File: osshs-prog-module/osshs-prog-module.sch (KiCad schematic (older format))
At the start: 2 parts, among them U1 STM32F103RETx

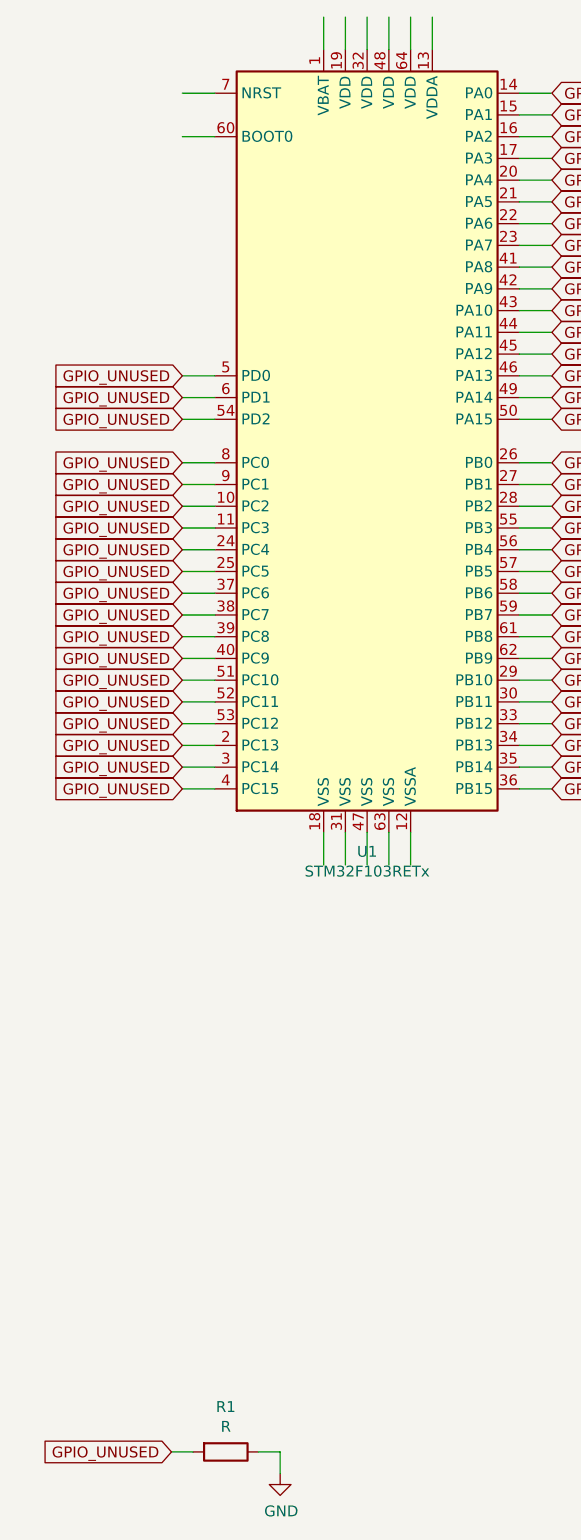
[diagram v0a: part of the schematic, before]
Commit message: [osshs-prog-module] Add reset circuit
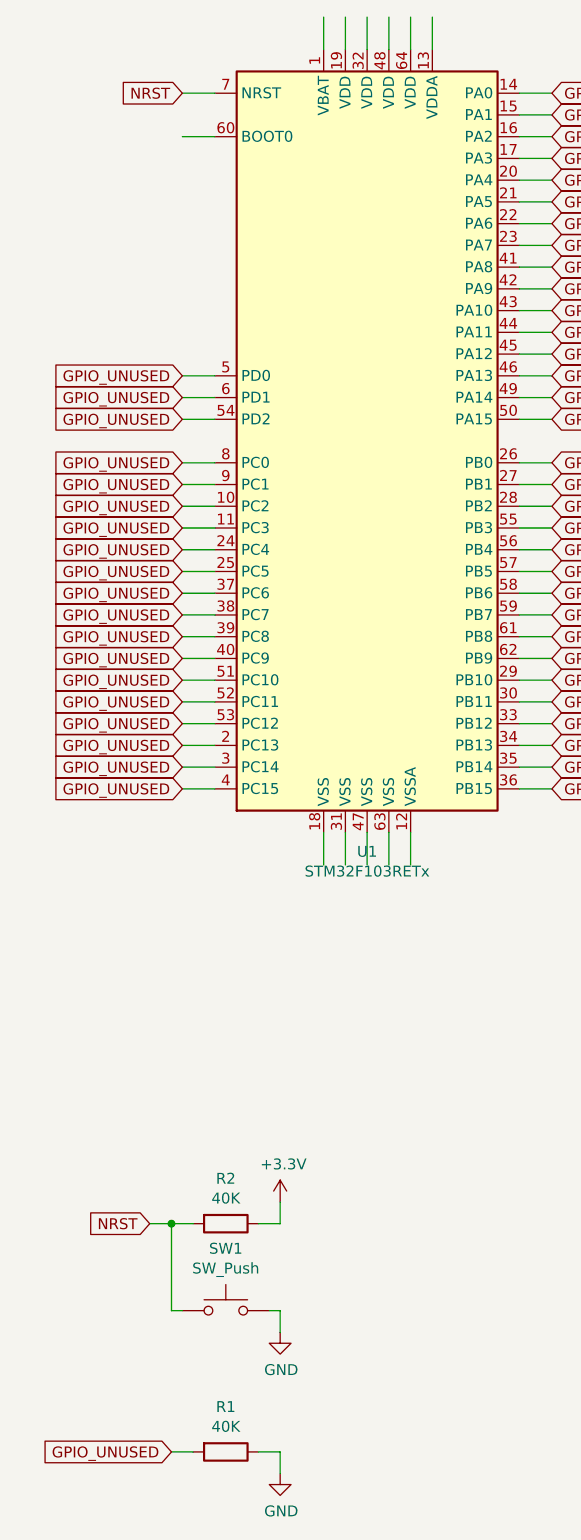
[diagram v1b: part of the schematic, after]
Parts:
- added R2: 40K, Resistor_SMD:R_0805_2012Metric, symbol Device:R
- added SW1: SW_Push, Button_Switch_SMD:SW_SPST_B3U-1000P, symbol Switch:SW_Push
- R1: value R -> 40K; footprint (none) -> Resistor_SMD:R_0805_2012Metric
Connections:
- net labels added: +3.3V, NRST
- wire segments 67 -> 75
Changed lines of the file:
@@
 EESchema Schematic File Version 4
+LIBS:osshs-prog-module-cache
 EELAYER 30 0
 EELAYER END
@@
 GPIO_UNUSED
 $Comp
+L Device:R R1
+U 1 1 5DEAE2F3
+P 1350 7450
+F 0 "R1" V 1143 7450 50  0000 C CNN
+F 1 "40K" V 1234 7450 50  0000 C CNN
+F 2 "Resistor_SMD:R_0805_2012Metric" V 1280 7450 50  0001 C CNN
+F 3 "~" H 1350 7450 50  0001 C CNN
+	1    1350 7450
+	0    1    1    0
+$EndComp
+Wire Wire Line
+	1100 7450 1200 7450
+Wire Wire Line
+	1500 7450 1600 7450
+Text GLabel 1150 1200 0    50   Input ~ 0
+NRST
+Text GLabel 1000 6400 0    50   Input ~ 0
+NRST
+$Comp
+L power:+3.3V #PWR0102
+U 1 1 5DE720C2
+P 1600 6300
+F 0 "#PWR0102" H 1600 6150 50  0001 C CNN
+F 1 "+3.3V" H 1615 6473 50  0000 C CNN
+F 2 "" H 1600 6300 50  0001 C CNN
+F 3 "" H 1600 6300 50  0001 C CNN
+	1    1600 6300
+	1    0    0    -1
+$EndComp
+$Comp
+L Device:R R2
+U 1 1 5DE7D093
+P 1350 6400
+F 0 "R2" V 1143 6400 50  0000 C CNN
+F 1 "40K" V 1234 6400 50  0000 C CNN
+F 2 "Resistor_SMD:R_0805_2012Metric" V 1280 6400 50  0001 C CNN
+F 3 "~" H 1350 6400 50  0001 C CNN
+	1    1350 6400
+	0    1    1    0
+$EndComp
+Wire Wire Line
+	1500 6400 1600 6400
+Wire Wire Line
+	1600 6400 1600 6300
+Wire Wire Line
+	1000 6400 1100 6400
+Connection ~ 1100 6400
+Wire Wire Line
+	1100 6400 1200 6400
+$Comp
+L Switch:SW_Push SW1
+U 1 1 5DE869D3
+P 1350 6800
+F 0 "SW1" H 1350 7085 50  0000 C CNN
+F 1 "SW_Push" H 1350 6994 50  0000 C CNN
+F 2 "Button_Switch_SMD:SW_SPST_B3U-1000P" H 1350 7000 50  0001 C CNN
+F 3 "~" H 1350 7000 50  0001 C CNN
+	1    1350 6800
+	1    0    0    -1
+$EndComp
+Wire Wire Line
+	1100 6800 1150 6800
+Wire Wire Line
+	1100 6400 1100 6800
+Wire Wire Line
+	1550 6800 1600 6800
+Wire Wire Line
+	1600 6800 1600 6900
+Wire Wire Line
+	1600 7450 1600 7550
+$Comp
 L power:GND #PWR0101
 U 1 1 5DEA1645
@@
 $EndComp
 $Comp
-L Device:R R1
-U 1 1 5DEAE2F3
-P 1350 7450
-F 0 "R1" V 1143 7450 50  0000 C CNN
-F 1 "R" V 1234 7450 50  0000 C CNN
-F 2 "" V 1280 7450 50  0001 C CNN
-F 3 "~" H 1350 7450 50  0001 C CNN
-	1    1350 7450
-	0    1    1    0
-$EndComp
-Wire Wire Line
-	1100 7450 1200 7450
-Wire Wire Line
-	1500 7450 1600 7450
-Wire Wire Line
-	1600 7450 1600 7550
+L power:GND #PWR0103
+U 1 1 5DE92E27
+P 1600 6900
+F 0 "#PWR0103" H 1600 6650 50  0001 C CNN
+F 1 "GND" H 1605 6727 50  0000 C CNN
+F 2 "" H 1600 6900 50  0001 C CNN
+F 3 "" H 1600 6900 50  0001 C CNN
+	1    1600 6900
+	1    0    0    -1
+$EndComp
 $EndSCHEMATC

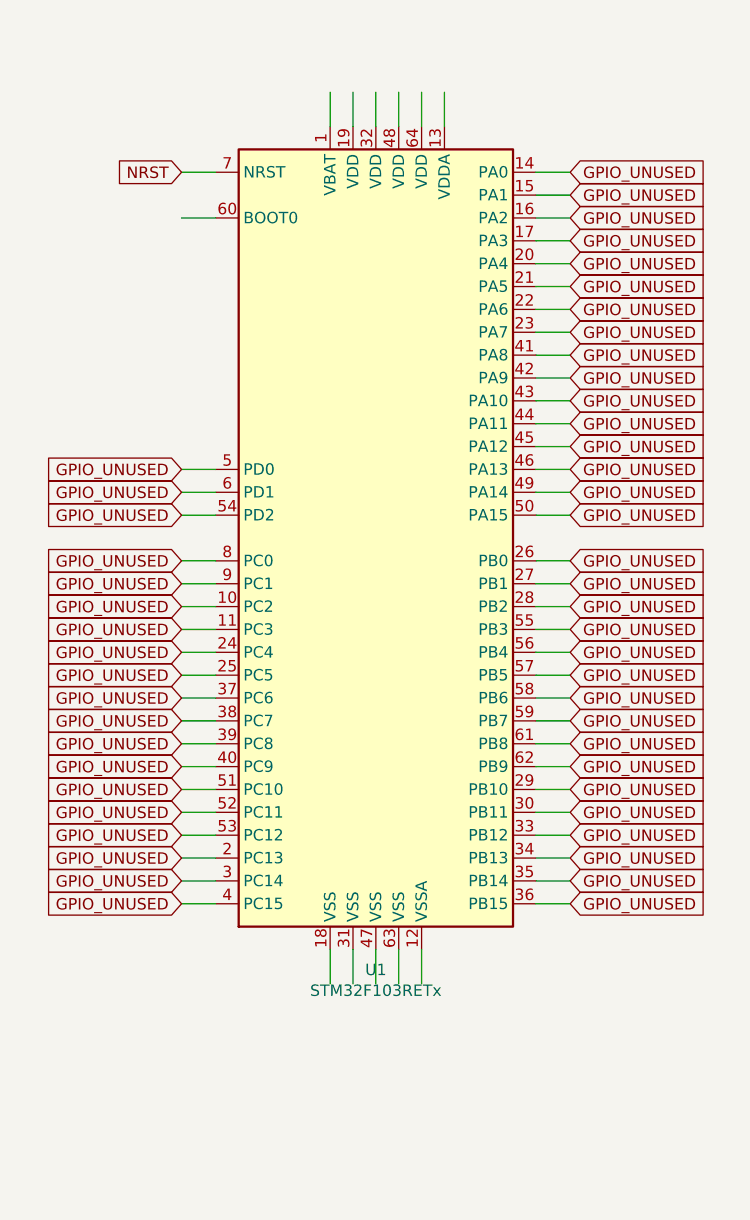
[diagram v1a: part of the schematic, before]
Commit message: [osshs-prog-module] Connect STM32 power pins
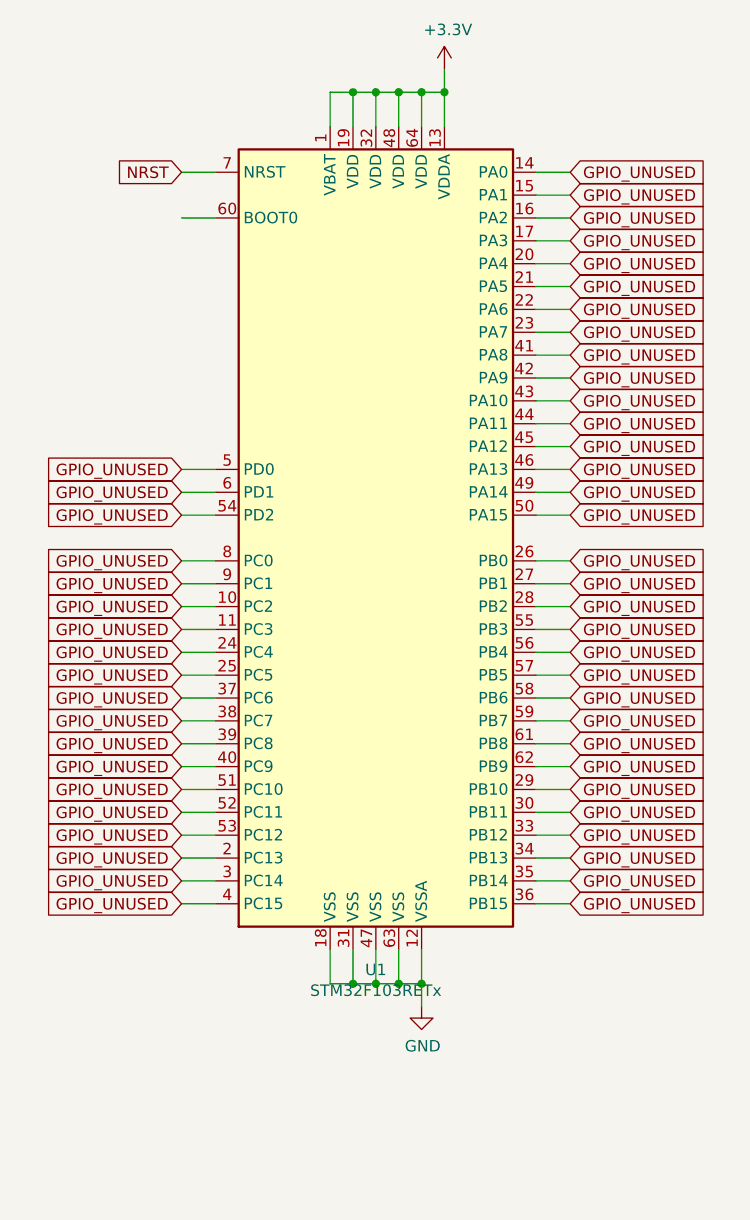
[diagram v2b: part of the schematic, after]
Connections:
- wire segments 75 -> 86
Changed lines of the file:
@@
+	1    0    0    -1
+$EndComp
+Wire Wire Line
+	1800 850  1900 850
+Wire Wire Line
+	1900 850  2000 850
+Connection ~ 1900 850
+Wire Wire Line
+	2000 850  2100 850
+Connection ~ 2000 850
+Wire Wire Line
+	2100 850  2200 850
+Connection ~ 2100 850
+Wire Wire Line
+	2200 850  2300 850
+Connection ~ 2200 850
+Wire Wire Line
+	2300 850  2300 750
+Connection ~ 2300 850
+$Comp
+L power:+3.3V #PWR?
+U 1 1 5DEAFF7F
+P 2300 750
+F 0 "#PWR?" H 2300 600 50  0001 C CNN
+F 1 "+3.3V" H 2315 923 50  0000 C CNN
+F 2 "" H 2300 750 50  0001 C CNN
+F 3 "" H 2300 750 50  0001 C CNN
+	1    2300 750
+	1    0    0    -1
+$EndComp
+Wire Wire Line
+	1800 4750 1900 4750
+Wire Wire Line
+	2000 4750 1900 4750
+Connection ~ 1900 4750
+Wire Wire Line
+	2000 4750 2100 4750
+Connection ~ 2000 4750
+Connection ~ 2100 4750
+Wire Wire Line
+	2100 4750 2200 4750
+Wire Wire Line
+	2200 4750 2200 4850
+Connection ~ 2200 4750
+$Comp
+L power:GND #PWR?
+U 1 1 5DEBBFB0
+P 2200 4850
+F 0 "#PWR?" H 2200 4600 50  0001 C CNN
+F 1 "GND" H 2205 4677 50  0000 C CNN
+F 2 "" H 2200 4850 50  0001 C CNN
+F 3 "" H 2200 4850 50  0001 C CNN
+	1    2200 4850
 	1    0    0    -1
 $EndComp

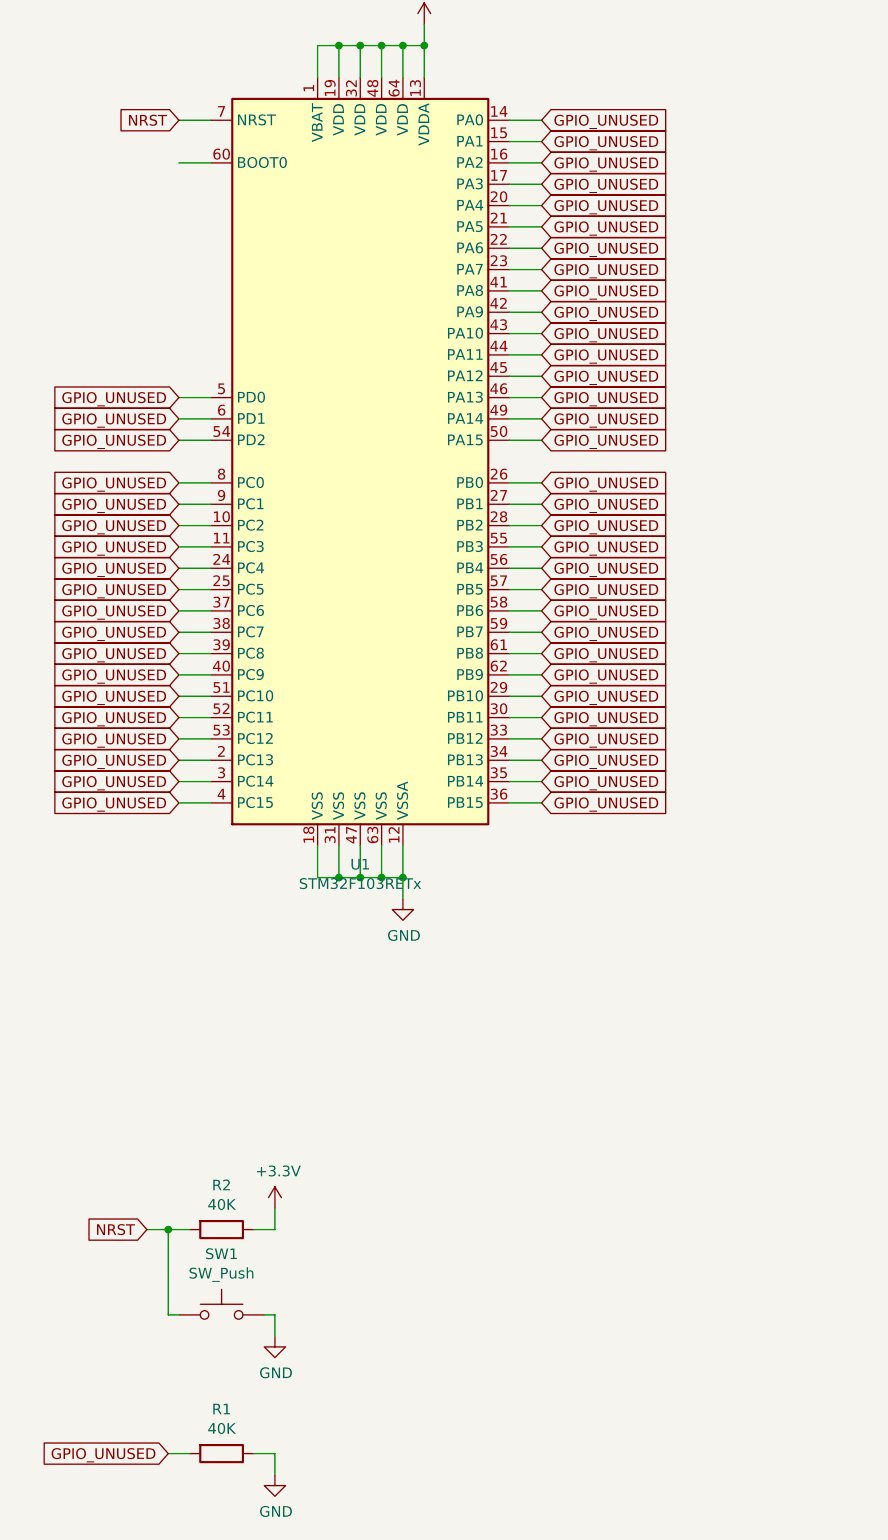
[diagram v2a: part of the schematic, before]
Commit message: [osshs-prog-module] Add boot mode selection circuit
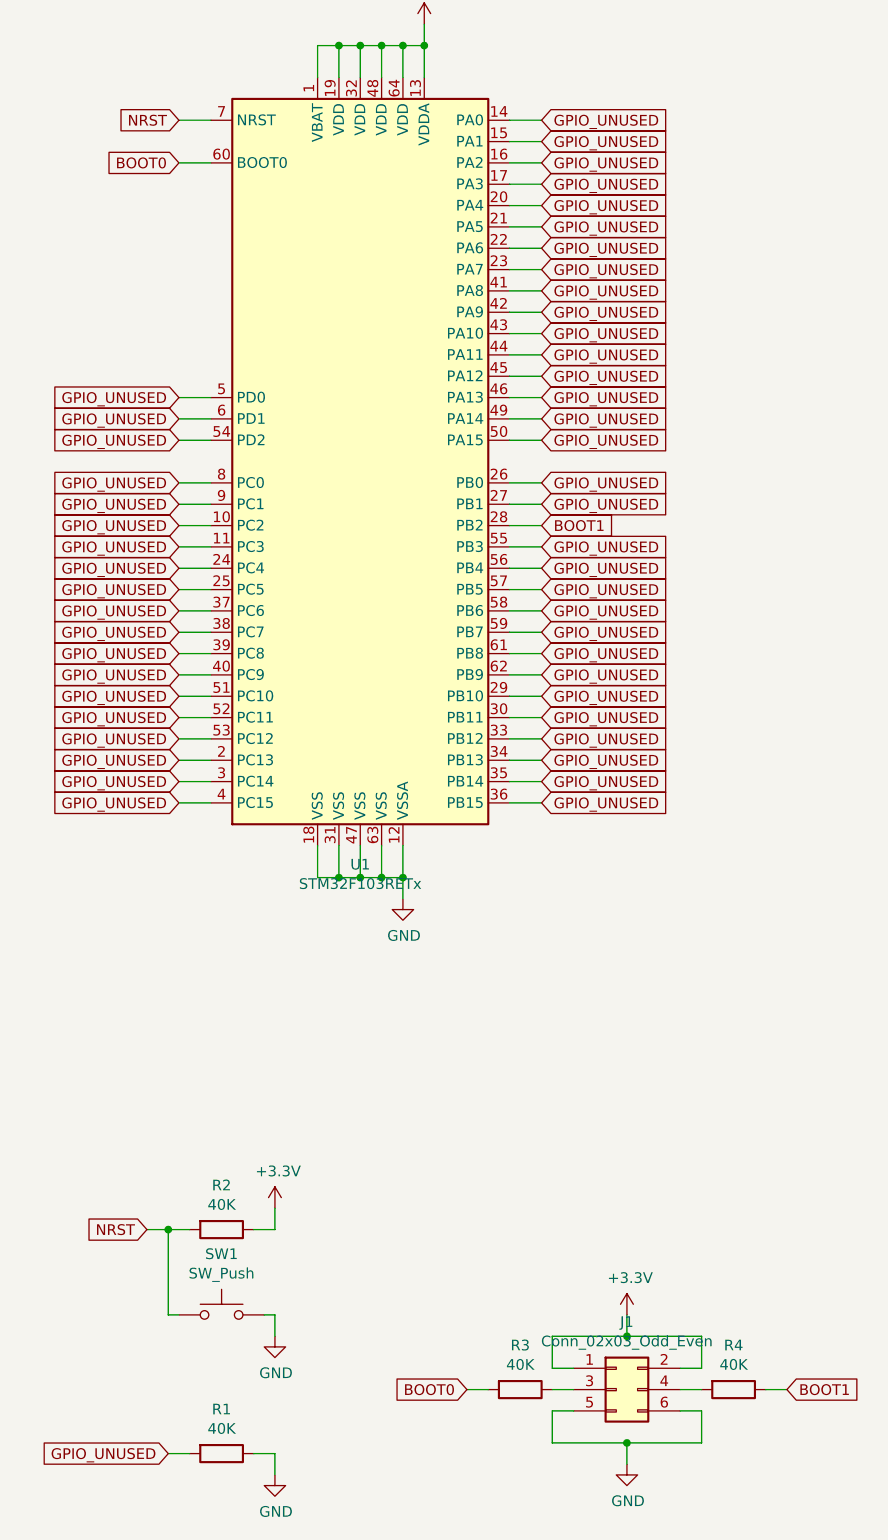
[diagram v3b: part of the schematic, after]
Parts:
- added J1: Conn_02x03_Odd_Even, Connector_PinHeader_2.54mm:PinHeader_2x03_P2.54mm_Vertical, symbol Connector_Generic:Conn_02x03_Odd_Even
- added R3, R4: 40K, Resistor_SMD:R_0805_2012Metric, symbol Device:R
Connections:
- net +3V3: now also J1.1 (Pin_1), J1.2 (Pin_2)
- net GND: now also J1.5 (Pin_5), J1.6 (Pin_6)
- net GPIO_UNUSED: no longer U1.28 (PB2)
- net BOOT0: now reaches U1.60 (BOOT0)
- net BOOT0: now also R3.2
- new net: J1.3 (Pin_3), R3.1
- new net: J1.4 (Pin_4), R4.2
- new net BOOT1: R4.1, U1.28 (PB2)
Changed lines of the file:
@@
 GPIO_UNUSED
 Text GLabel 2850 3100 2    50   Input ~ 0
-GPIO_UNUSED
+BOOT1
 Text GLabel 2850 3200 2    50   Input ~ 0
 GPIO_UNUSED
@@
 Connection ~ 2300 850
 $Comp
-L power:+3.3V #PWR?
+L power:+3.3V #PWR0104
 U 1 1 5DEAFF7F
 P 2300 750
-F 0 "#PWR?" H 2300 600 50  0001 C CNN
+F 0 "#PWR0104" H 2300 600 50  0001 C CNN
 F 1 "+3.3V" H 2315 923 50  0000 C CNN
 F 2 "" H 2300 750 50  0001 C CNN
@@
 Connection ~ 2200 4750
 $Comp
-L power:GND #PWR?
+L power:GND #PWR0105
 U 1 1 5DEBBFB0
 P 2200 4850
-F 0 "#PWR?" H 2200 4600 50  0001 C CNN
+F 0 "#PWR0105" H 2200 4600 50  0001 C CNN
 F 1 "GND" H 2205 4677 50  0000 C CNN
 F 2 "" H 2200 4850 50  0001 C CNN
@@
 	1    0    0    -1
 $EndComp
+Text GLabel 1150 1400 0    50   Input ~ 0
+BOOT0
+$Comp
+L Connector_Generic:Conn_02x03_Odd_Even J1
+U 1 1 5DECC2C7
+P 3200 7150
+F 0 "J1" H 3250 7467 50  0000 C CNN
+F 1 "Conn_02x03_Odd_Even" H 3250 7376 50  0000 C CNN
+F 2 "Connector_PinHeader_2.54mm:PinHeader_2x03_P2.54mm_Vertical" H 3200 7150 50  0001 C CNN
+F 3 "~" H 3200 7150 50  0001 C CNN
+	1    3200 7150
+	1    0    0    -1
+$EndComp
+Wire Wire Line
+	3500 7050 3600 7050
+Wire Wire Line
+	3600 7050 3600 6900
+Wire Wire Line
+	2900 6900 2900 7050
+Wire Wire Line
+	2900 7050 3000 7050
+Wire Wire Line
+	2900 6900 3250 6900
+Wire Wire Line
+	3000 7250 2900 7250
+Wire Wire Line
+	2900 7250 2900 7400
+Wire Wire Line
+	2900 7400 3250 7400
+Wire Wire Line
+	3600 7400 3600 7250
+Wire Wire Line
+	3600 7250 3500 7250
+Wire Wire Line
+	3250 7400 3250 7500
+Connection ~ 3250 7400
+Wire Wire Line
+	3250 7400 3600 7400
+Wire Wire Line
+	3250 6900 3250 6800
+Connection ~ 3250 6900
+Wire Wire Line
+	3250 6900 3600 6900
+$Comp
+L power:+3.3V #PWR0106
+U 1 1 5DED9DD9
+P 3250 6800
+F 0 "#PWR0106" H 3250 6650 50  0001 C CNN
+F 1 "+3.3V" H 3265 6973 50  0000 C CNN
+F 2 "" H 3250 6800 50  0001 C CNN
+F 3 "" H 3250 6800 50  0001 C CNN
+	1    3250 6800
+	1    0    0    -1
+$EndComp
+$Comp
+L power:GND #PWR0107
+U 1 1 5DEDA21B
+P 3250 7500
+F 0 "#PWR0107" H 3250 7250 50  0001 C CNN
+F 1 "GND" H 3255 7327 50  0000 C CNN
+F 2 "" H 3250 7500 50  0001 C CNN
+F 3 "" H 3250 7500 50  0001 C CNN
+	1    3250 7500
+	1    0    0    -1
+$EndComp
+$Comp
+L Device:R R3
+U 1 1 5DEDABE6
+P 2750 7150
+F 0 "R3" V 2543 7150 50  0000 C CNN
+F 1 "40K" V 2634 7150 50  0000 C CNN
+F 2 "Resistor_SMD:R_0805_2012Metric" V 2680 7150 50  0001 C CNN
+F 3 "~" H 2750 7150 50  0001 C CNN
+	1    2750 7150
+	0    1    1    0
+$EndComp
+$Comp
+L Device:R R4
+U 1 1 5DEDE2CE
+P 3750 7150
+F 0 "R4" V 3543 7150 50  0000 C CNN
+F 1 "40K" V 3634 7150 50  0000 C CNN
+F 2 "Resistor_SMD:R_0805_2012Metric" V 3680 7150 50  0001 C CNN
+F 3 "~" H 3750 7150 50  0001 C CNN
+	1    3750 7150
+	0    1    1    0
+$EndComp
+Wire Wire Line
+	3500 7150 3600 7150
+Wire Wire Line
+	2900 7150 3000 7150
+Wire Wire Line
+	3900 7150 4000 7150
+Wire Wire Line
+	2600 7150 2500 7150
+Text GLabel 2500 7150 0    50   Input ~ 0
+BOOT0
+Text GLabel 4000 7150 2    50   Input ~ 0
+BOOT1
 $EndSCHEMATC
